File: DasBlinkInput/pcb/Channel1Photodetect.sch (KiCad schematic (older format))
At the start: 11 parts, among them P201 TP_CHAN1, U201 MCP6404, U202 LM339

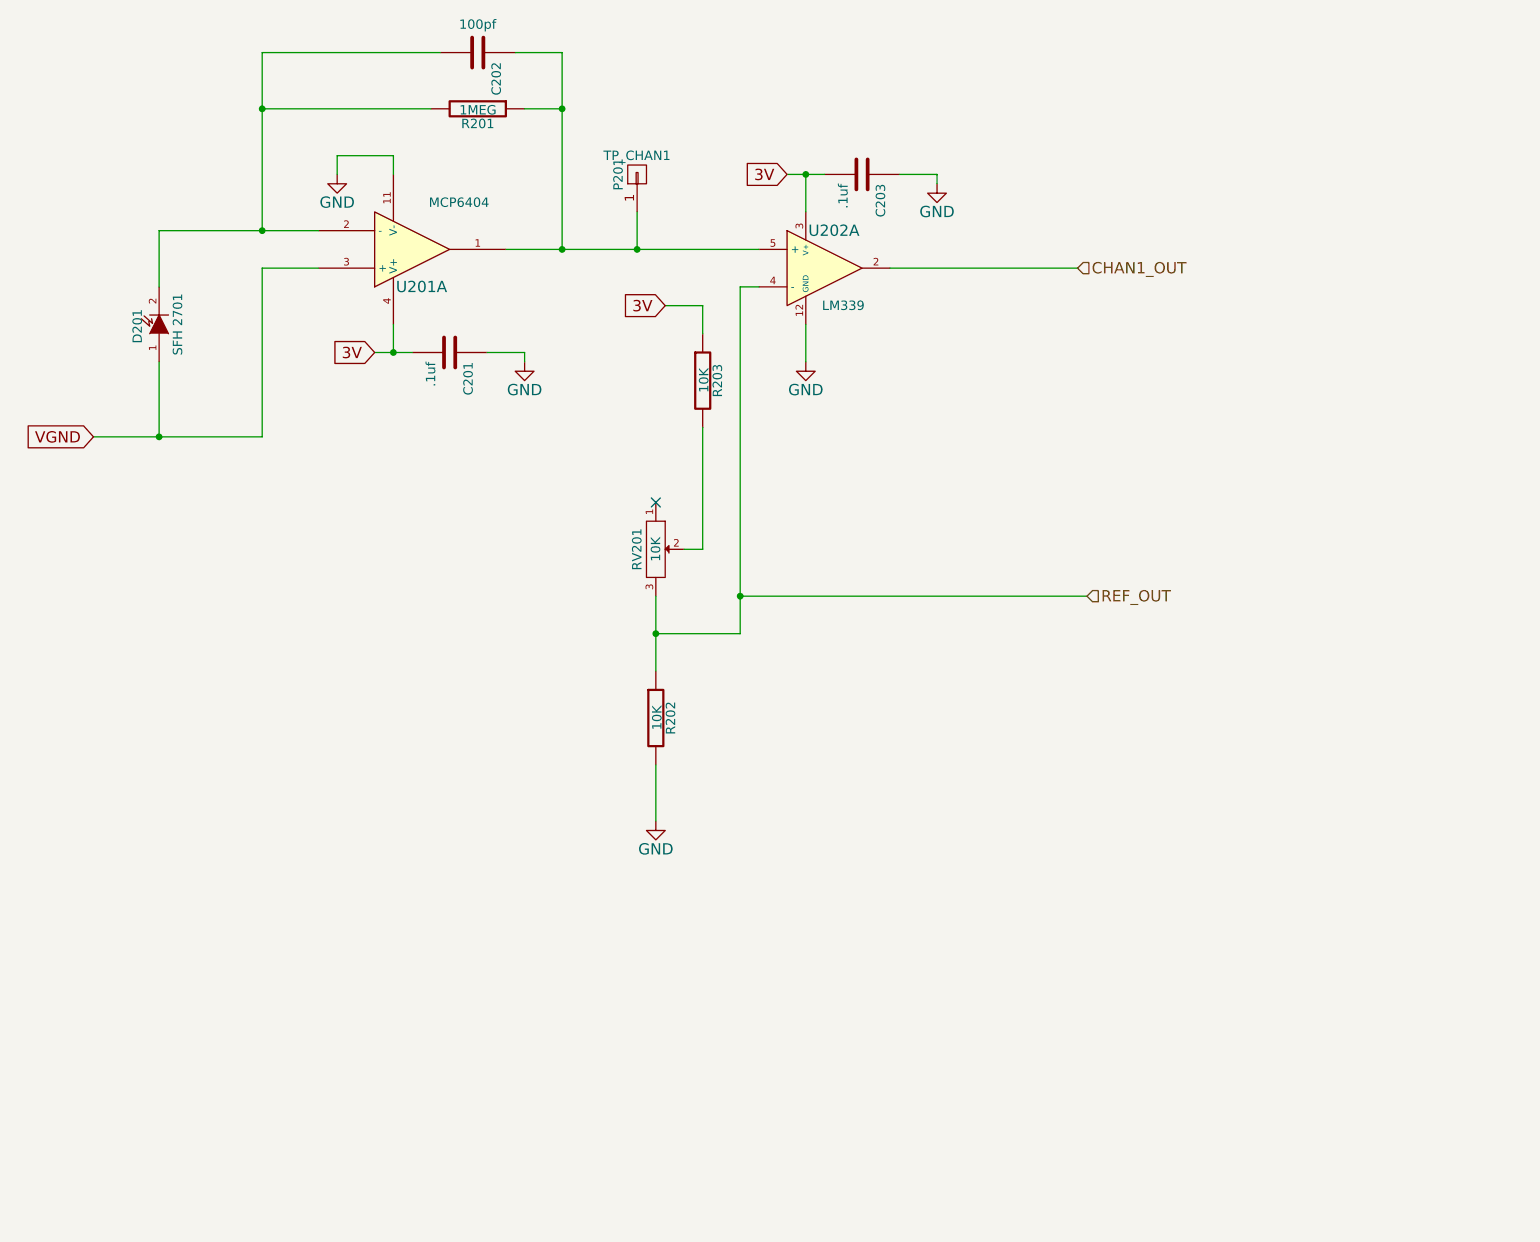
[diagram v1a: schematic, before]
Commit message: DBI - fixed reg/on pin, changed resistor to 0 ohm near divider and rv, added 10k pull up resistors to 3V for each output channel.
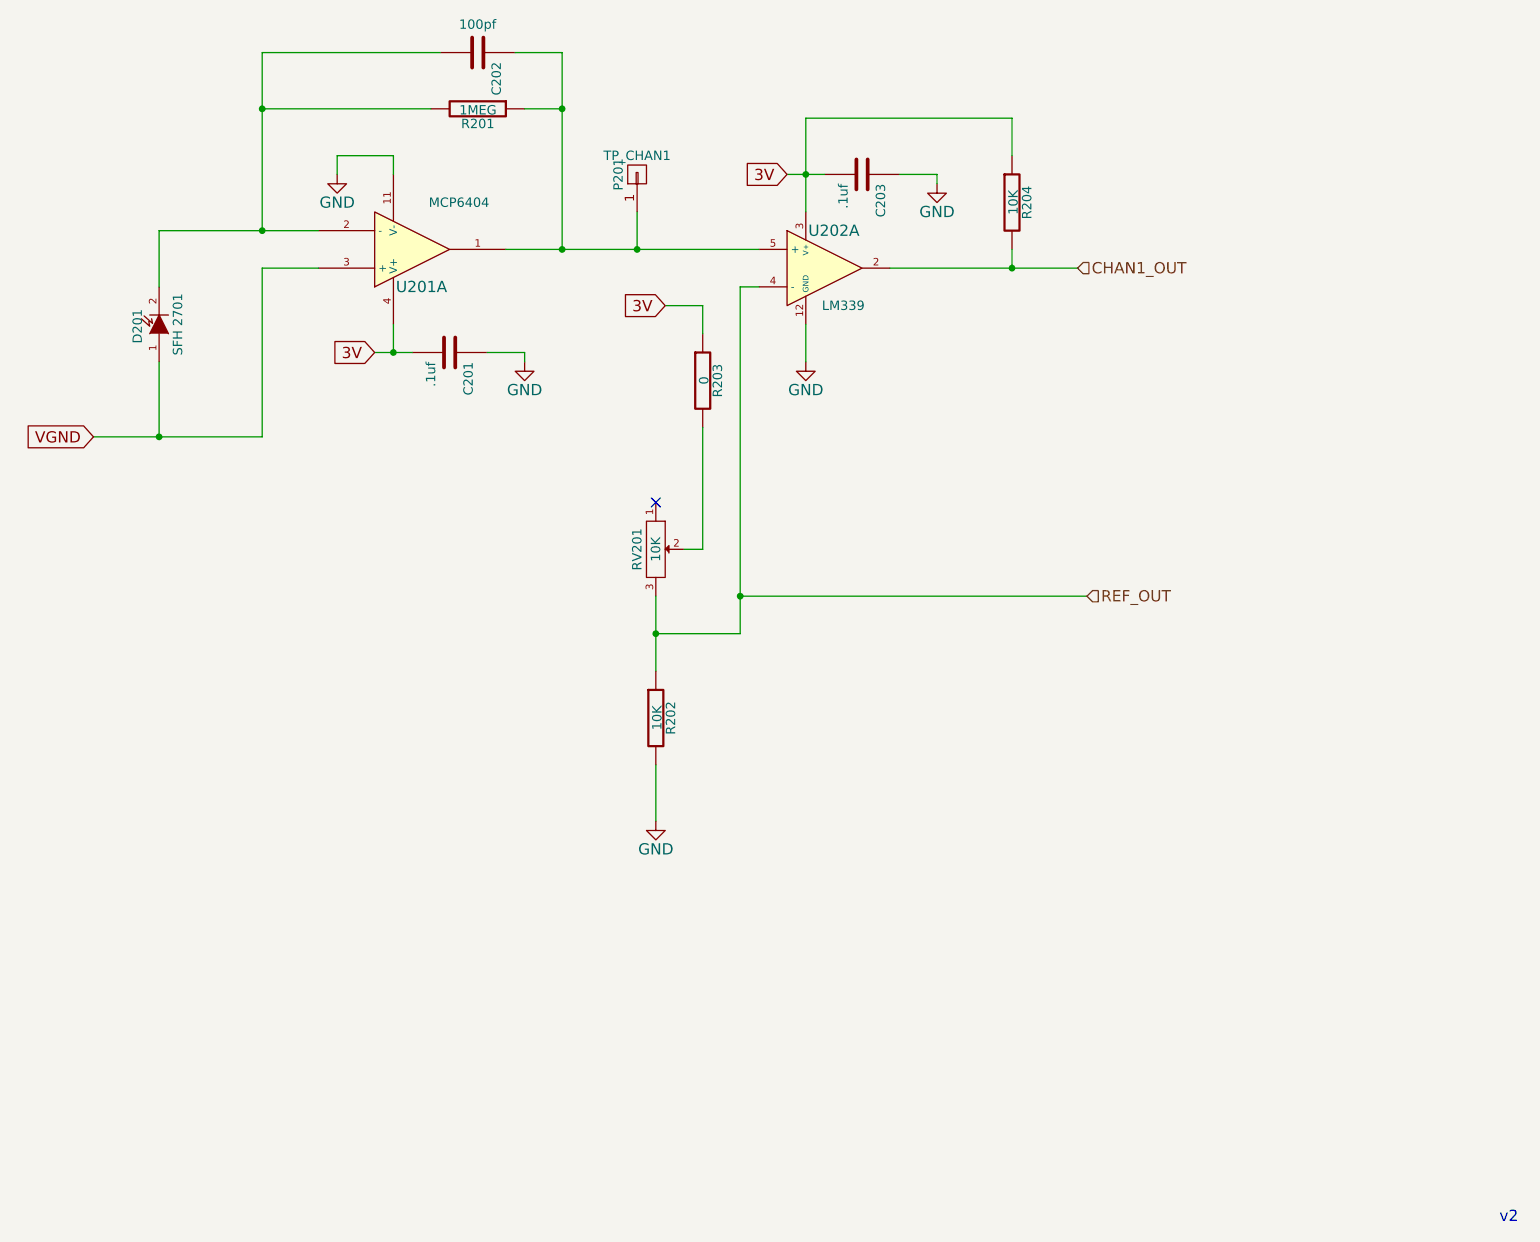
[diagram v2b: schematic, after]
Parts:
- added R204: 10K, Resistors_SMD:R_0805_HandSoldering, symbol R
- R203: value 10K -> 0
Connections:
- net 3V: now also R204.1
- net CHAN1_OUT: now also R204.2
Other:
- note added: "v2"
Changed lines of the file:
@@
 P 6350 3150
 F 0 "R203" V 6430 3150 50  0000 C CNN
-F 1 "10K" V 6357 3151 50  0000 C CNN
+F 1 "0" V 6357 3151 50  0000 C CNN
 F 2 "Resistors_SMD:R_0805_HandSoldering" V 6280 3150 30  0001 C CNN
 F 3 "" H 6350 3150 30  0000 C CNN
@@
 	6550 2650 6550 4500
 Wire Wire Line
-	6100 4300 6100 4700
-Wire Wire Line
 	6550 4500 6100 4500
-Connection ~ 6100 4500
 Wire Wire Line
 	6350 4050 6250 4050
@@
 	7600 2050 7600 2100
 Wire Wire Line
-	6900 2050 6900 2250
+	6900 1750 6900 2250
 $Comp
 L GND #PWR09
@@
 Connection ~ 6000 2450
 NoConn ~ 6100 3800
+Wire Wire Line
+	6100 4300 6100 4700
+Connection ~ 6100 4500
+Text Notes 10600 7650 0    60   ~ 0
+v2
+$Comp
+L R R204
+U 1 1 55B599B2
+P 8000 2200
+F 0 "R204" V 8080 2200 50  0000 C CNN
+F 1 "10K" V 8007 2201 50  0000 C CNN
+F 2 "Resistors_SMD:R_0805_HandSoldering" V 7930 2200 30  0001 C CNN
+F 3 "" H 8000 2200 30  0000 C CNN
+	1    8000 2200
+	1    0    0    -1
+$EndComp
+Wire Wire Line
+	8000 2550 8000 2450
+Connection ~ 8000 2550
+Wire Wire Line
+	8000 1950 8000 1750
+Wire Wire Line
+	8000 1750 6900 1750
 $EndSCHEMATC
